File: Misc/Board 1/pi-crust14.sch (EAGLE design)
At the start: 49 parts, among them IC10 40193N, IC2 74LS595D, IC3 74LS595D, IC4 74LS595D, IC5 74LS595D, IC6 74LS595D, IC7 74LS595D, IC8 74AC11008, U1 AD9983AKSTZ_140, U2 SN54LS253_J_16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

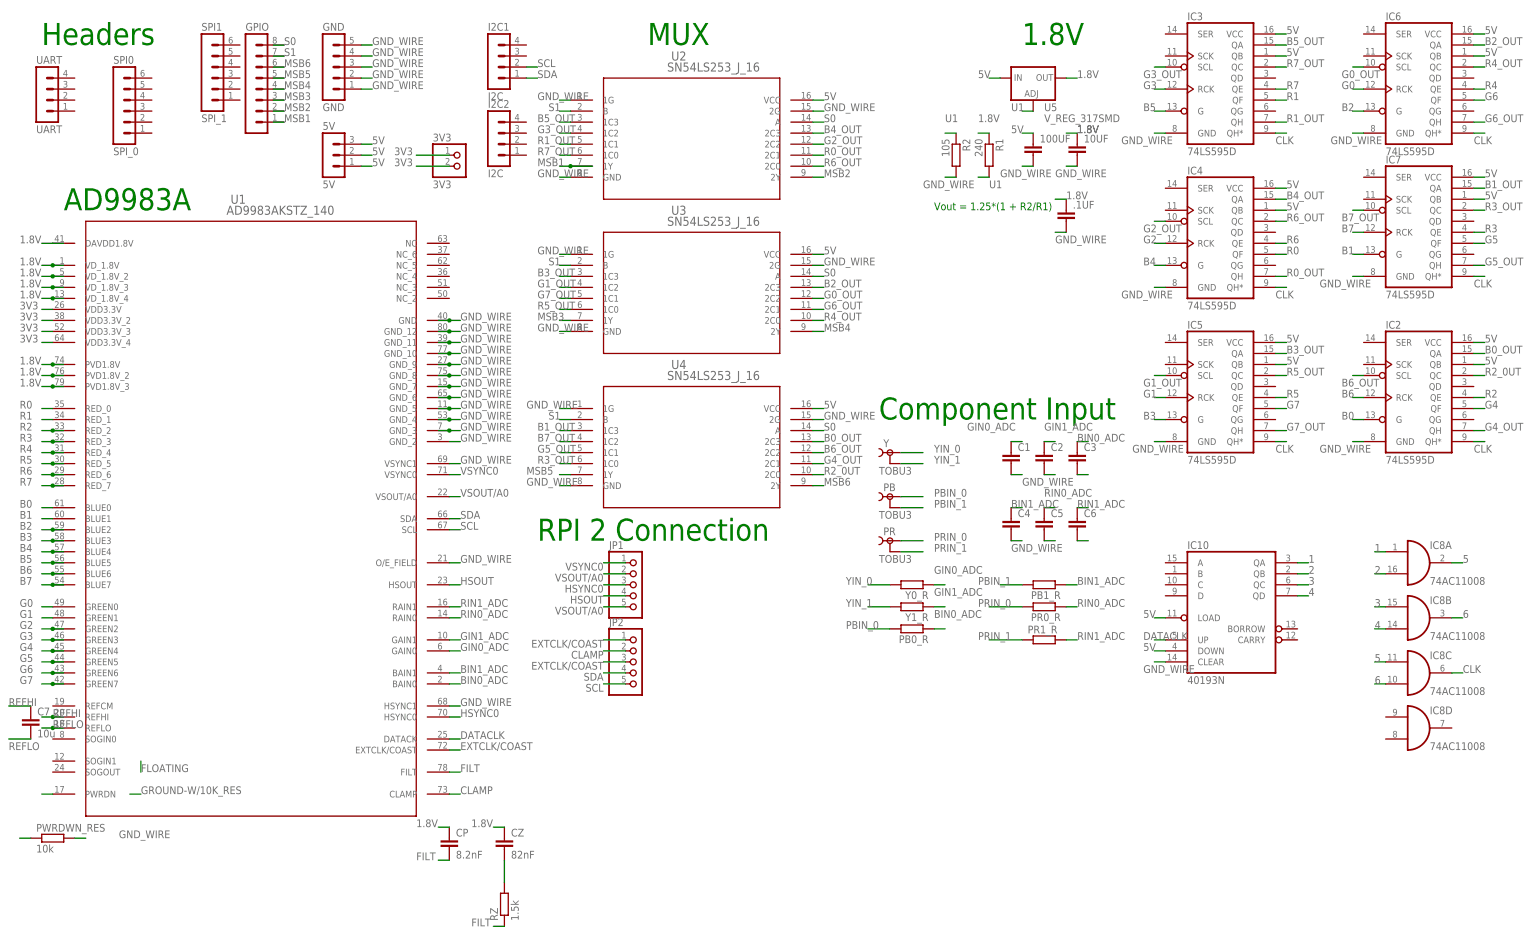
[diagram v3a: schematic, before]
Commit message: Board Update 7
Rather than using the TOBU3, I have used a 1x1 pin header and used the
dimensions of RCJ-32265 (our RCA jack).  I also had to move some
resistors and capacitors around because of the order of input.  All else
remains the same as in 14
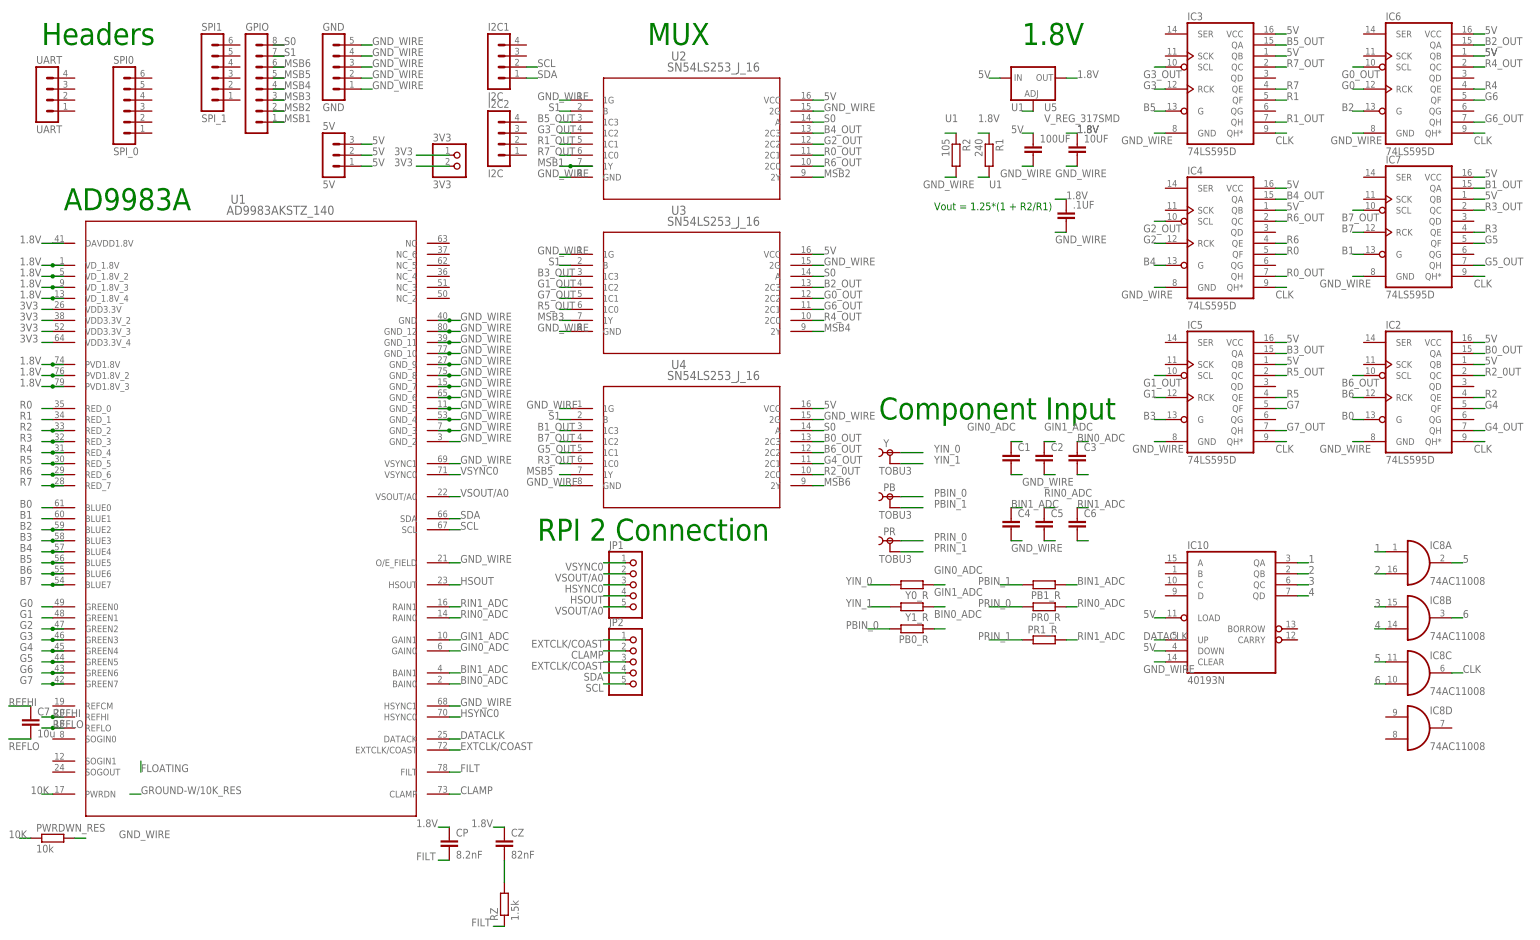
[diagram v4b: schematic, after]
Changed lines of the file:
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@@
 <wire x1="337.82" y1="175.26" x2="335.28" y2="175.26" width="0.6096" layer="91"/>
 <pinref part="IC6" gate="A" pin="QB"/>
+<label x="337.82" y="175.26" size="1.778" layer="95"/>
 </segment>
 <segment>
@@
 <pinref part="U1" gate="A" pin="PWRDN"/>
 <wire x1="7.62" y1="5.08" x2="5.08" y2="5.08" width="0.6096" layer="91"/>
+<label x="2.54" y="5.08" size="1.778" layer="95"/>
 </segment>
 <segment>
 <wire x1="2.54" y1="-5.08" x2="0" y2="-5.08" width="0.6096" layer="91"/>
 <pinref part="PWRDWN_RES" gate="G$1" pin="1"/>
-</segment>
-</net>
+<label x="-2.54" y="-5.08" size="1.778" layer="95"/>
+</segment>
+</net>
